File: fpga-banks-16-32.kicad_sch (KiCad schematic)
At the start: 1 part, among them U1 XC7K410T-2FFG900I

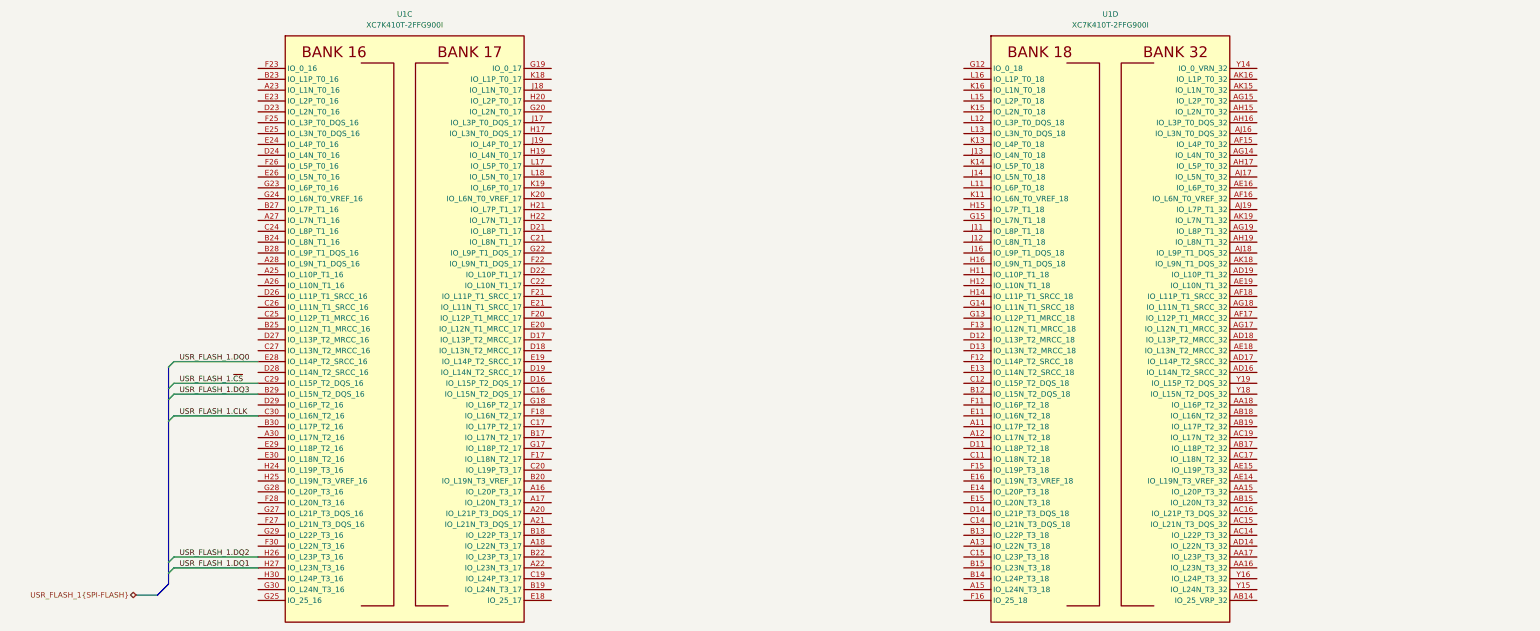
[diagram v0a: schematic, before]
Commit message: Connect user USB to FPGA. Connect RMII, usr USB and usr SPI Flash 1 on root sheet
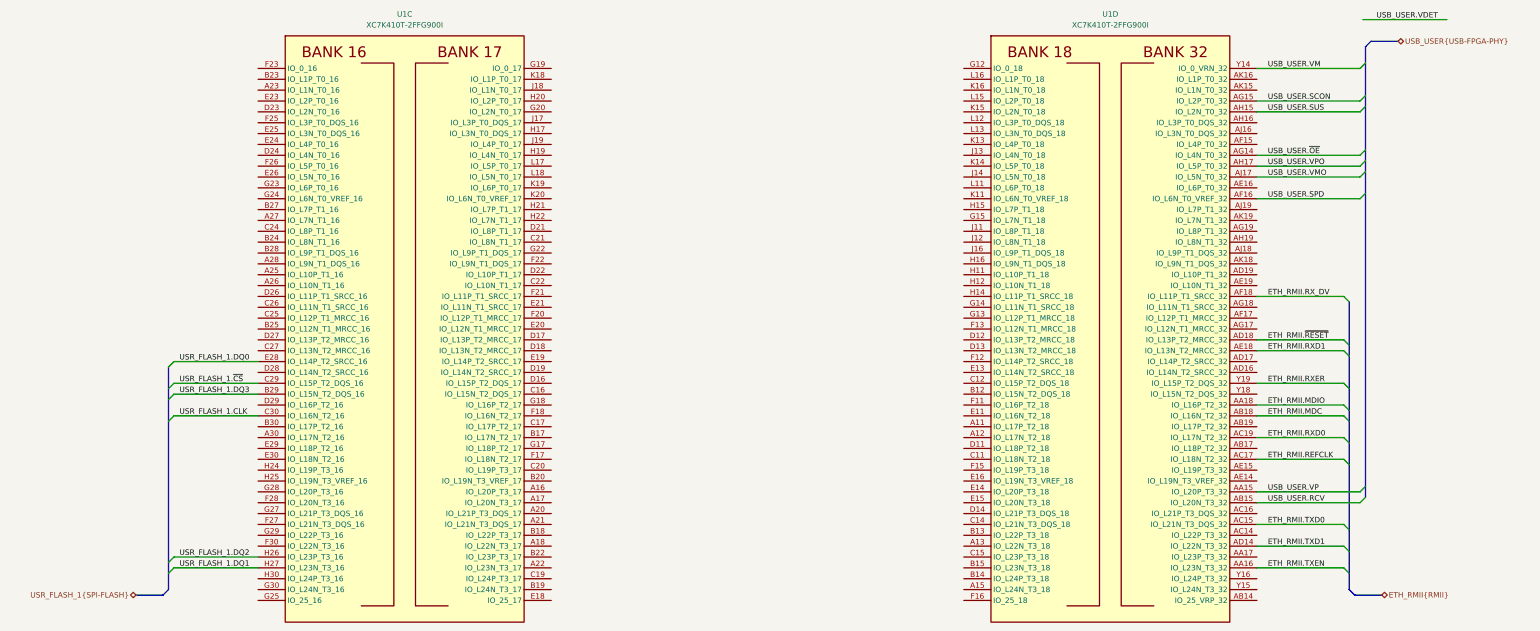
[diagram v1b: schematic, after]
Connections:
- net USB_USER.VP: now reaches U1.AA15 (IO_L20P_T3_32)
- net ETH_RMII.TXEN: now reaches U1.AA16 (IO_L23N_T3_32)
- net ETH_RMII.MDIO: now reaches U1.AA18 (IO_L16P_T2_32)
- net USB_USER.RCV: now reaches U1.AB15 (IO_L20N_T3_32)
- net ETH_RMII.MDC: now reaches U1.AB18 (IO_L16N_T2_32)
- net ETH_RMII.TXD0: now reaches U1.AC15 (IO_L21N_T3_DQS_32)
- net ETH_RMII.REFCLK: now reaches U1.AC17 (IO_L18N_T2_32)
- net ETH_RMII.RXD0: now reaches U1.AC19 (IO_L17N_T2_32)
- net ETH_RMII.TXD1: now reaches U1.AD14 (IO_L22N_T3_32)
- net ETH_RMII.~{RESET}: now reaches U1.AD18 (IO_L13P_T2_MRCC_32)
- net ETH_RMII.RXD1: now reaches U1.AE18 (IO_L13N_T2_MRCC_32)
- net USB_USER.SPD: now reaches U1.AF16 (IO_L6N_T0_VREF_32)
- net ETH_RMII.RX_DV: now reaches U1.AF18 (IO_L11P_T1_SRCC_32)
- net USB_USER.~{OE}: now reaches U1.AG14 (IO_L4N_T0_32)
- net USB_USER.SCON: now reaches U1.AG15 (IO_L2P_T0_32)
- net USB_USER.SUS: now reaches U1.AH15 (IO_L2N_T0_32)
- net USB_USER.VPO: now reaches U1.AH17 (IO_L5P_T0_32)
- net USB_USER.VMO: now reaches U1.AJ17 (IO_L5N_T0_32)
- net USB_USER.VM: now reaches U1.Y14 (IO_0_VRN_32)
- net ETH_RMII.RXER: now reaches U1.Y19 (IO_L15P_T2_DQS_32)
